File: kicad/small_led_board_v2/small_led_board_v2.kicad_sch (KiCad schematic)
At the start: 89 parts, among them Q1 SQ2351CES, Q2 SQ2351CES, Q3 SQ2351CES, Q4 SQ2351CES, Q5 SQ2351CES, Q6 SQ2351CES, U1 74HCT541, U2 74HCT595, U3 TPIC6B595N

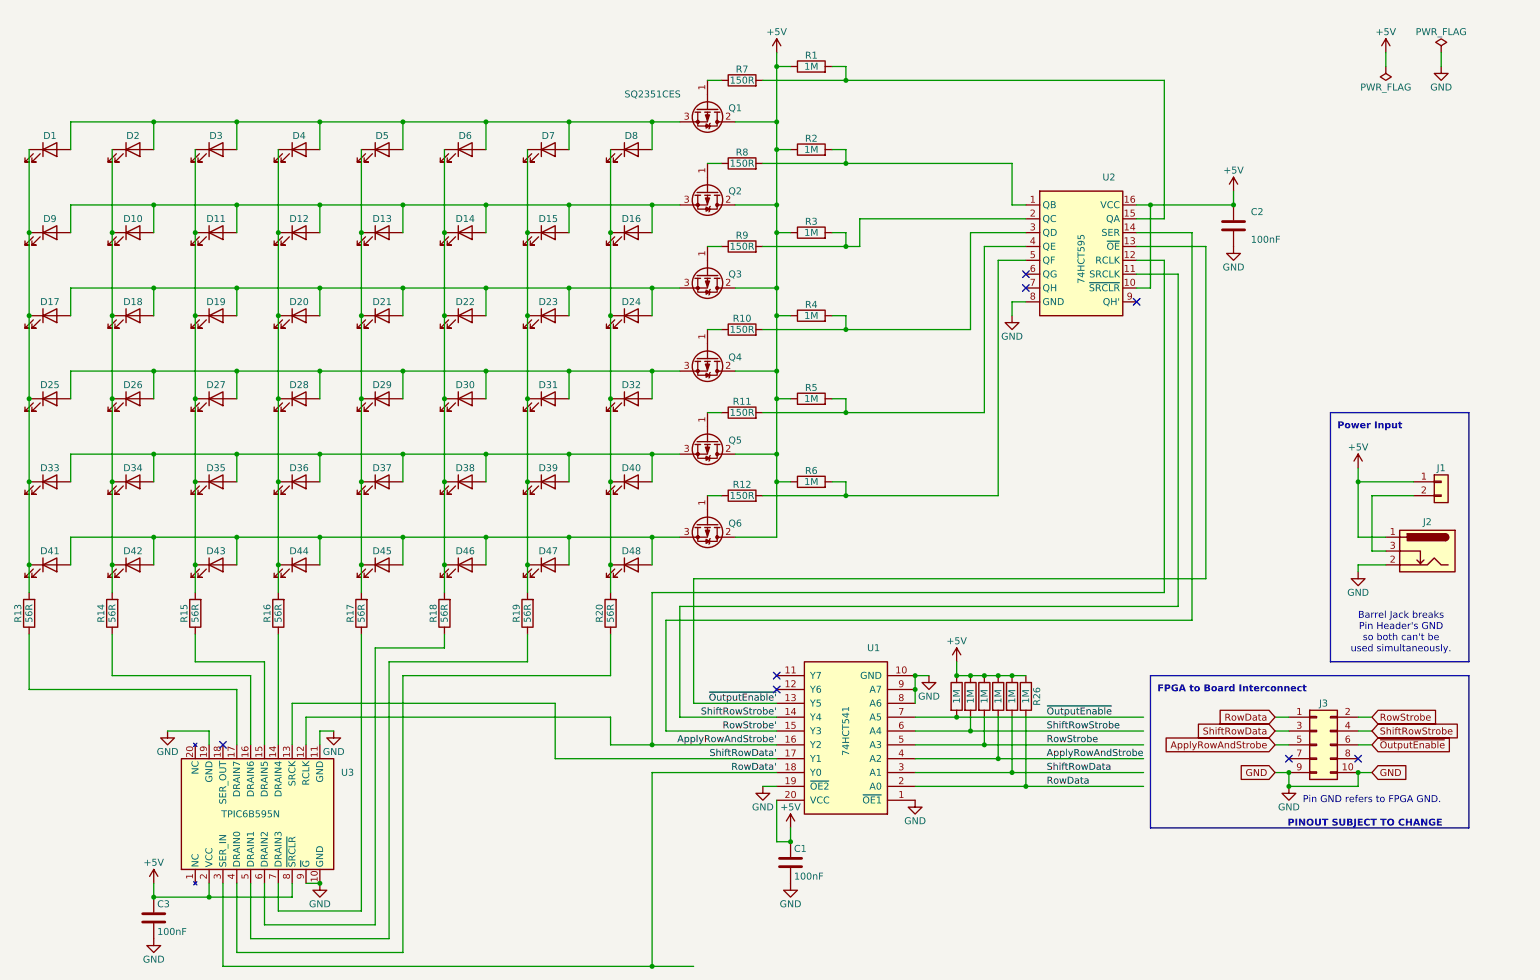
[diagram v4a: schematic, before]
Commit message: small led board v2: replaced rect+text with text box
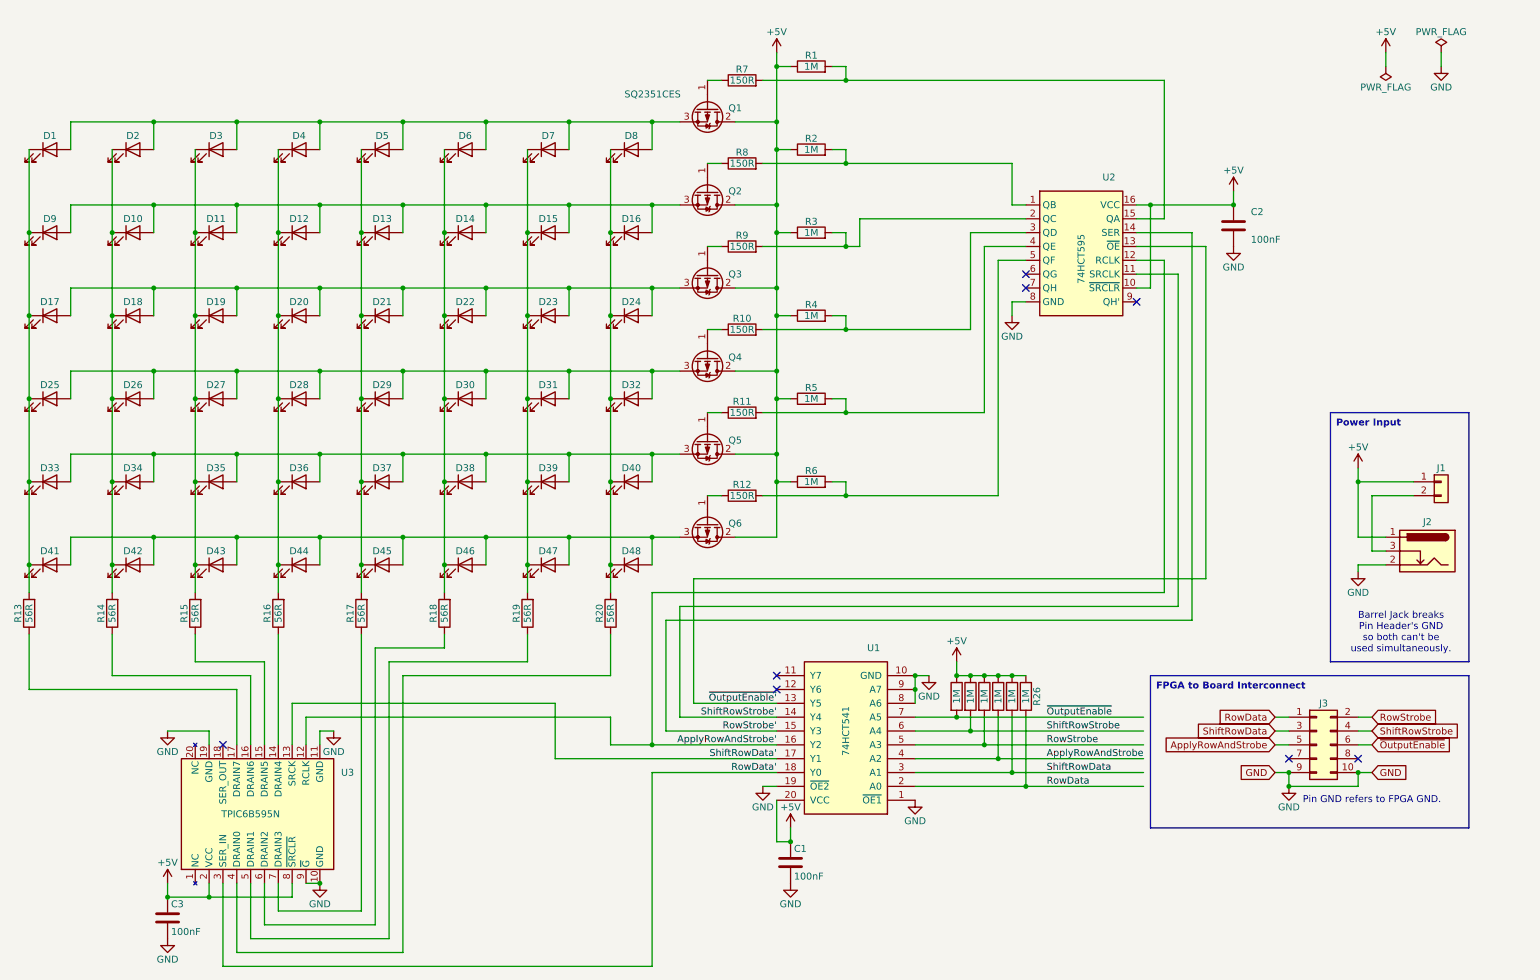
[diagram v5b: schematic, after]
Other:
- note removed: "FPGA to Board Interconnect"
- note removed: "PINOUT SUBJECT TO CHANGE"
- note removed: "Power Input"
- moved on the sheet: C3
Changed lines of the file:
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@@
 	)
 	(junction
-		(at 132.08 187.96)
-		(diameter 0)
-		(color 0 0 0 0)
-	)
-	(junction
 		(at 132.08 109.22)
 		(diameter 0)
@@
 	)
 	(junction
-		(at 40.64 175.26)
+		(at 43.18 175.26)
 		(diameter 0)
 		(color 0 0 0 0)
@@
 	(wire
 		(pts
-			(xy 40.64 172.72) (xy 40.64 175.26)
+			(xy 43.18 172.72) (xy 43.18 175.26)
 		)
 		(stroke
@@
 	(wire
 		(pts
-			(xy 40.64 175.26) (xy 50.8 175.26)
+			(xy 43.18 175.26) (xy 50.8 175.26)
 		)
 		(stroke
@@
 	(wire
 		(pts
-			(xy 132.08 187.96) (xy 139.7 187.96)
-		)
-		(stroke
-			(width 0)
-			(type default)
-		)
-	)
-	(wire
-		(pts
 			(xy 180.34 142.24) (xy 187.96 142.24)
 		)
@@
 		)
 	)
-	(rectangle
-		(start 256.54 86.36)
-		(end 281.94 132.08)
-		(stroke
-			(width 0)
-			(type default)
-		)
-		(fill
-			(type none)
-		)
-	)
-	(rectangle
-		(start 223.52 134.62)
-		(end 281.94 162.56)
+	(text_box "FPGA to Board Interconnect"
+		(exclude_from_sim no)
+		(at 223.52 134.62 0)
+		(size 58.42 27.94)
 		(stroke
 			(width 0)
@@
 			(type none)
 		)
-	)
-	(text "PINOUT SUBJECT TO CHANGE"
-		(exclude_from_sim no)
-		(at 262.89 161.798 0)
 		(effects
 			(font
 				(size 1.27 1.27)
+				(thickness 0.254)
 				(bold yes)
 			)
+			(justify left top)
 		)
 	)
-	(text "Power Input"
+	(text_box "Power Input"
 		(exclude_from_sim no)
-		(at 257.81 88.9 0)
+		(at 256.54 86.36 0)
+		(size 25.4 45.72)
+		(stroke
+			(width 0)
+			(type default)
+		)
+		(fill
+			(type none)
+		)
 		(effects
 			(font
 				(size 1.27 1.27)
-				(thickness 0.254)
 				(bold yes)
 			)
-			(justify left)
+			(justify left top)
 		)
 	)
@@
 		)
 	)
-	(text "FPGA to Board Interconnect"
-		(exclude_from_sim no)
-		(at 224.79 137.16 0)
-		(effects
-			(font
-				(size 1.27 1.27)
-				(thickness 0.254)
-				(bold yes)
-			)
-			(justify left)
-		)
-	)
 	(text "Pin GND refers to FPGA GND."
 		(exclude_from_sim no)
@@
 	(symbol
 		(lib_id "Device:C")
-		(at 40.64 179.07 0)
+		(at 43.18 179.07 0)
 		(unit 1)
 		(exclude_from_sim no)
@@
 		(fields_autoplaced yes)
 		(property "Reference" "C3"
-			(at 41.275 176.53 0)
+			(at 43.815 176.53 0)
 			(effects
 				(font
@@
 		)
 		(property "Value" "100nF"
-			(at 41.275 181.61 0)
+			(at 43.815 181.61 0)
 			(effects
 				(font
@@
 		)
 		(property "Footprint" "Capacitor_THT:C_Disc_D4.7mm_W2.5mm_P5.00mm"
-			(at 41.6052 182.88 0)
+			(at 44.1452 182.88 0)
 			(effects
 				(font
@@
 		)
 		(property "Datasheet" "~"
-			(at 40.64 179.07 0)
+			(at 43.18 179.07 0)
 			(effects
 				(font
@@
 		)
 		(property "Description" "Unpolarized capacitor"
-			(at 40.64 179.07 0)
+			(at 43.18 179.07 0)
 			(effects
 				(font
@@
 	(symbol
 		(lib_id "power:GND")
-		(at 40.64 182.88 0)
+		(at 43.18 182.88 0)
 		(unit 1)
 		(exclude_from_sim no)
@@
 		(fields_autoplaced yes)
 		(property "Reference" "#PWR0115"
-			(at 40.64 189.23 0)
+			(at 43.18 189.23 0)
 			(effects
 				(font
@@
 		)
 		(property "Value" "GND"
-			(at 40.64 186.69 0)
+			(at 43.18 186.69 0)
 			(effects
 				(font
@@
 		)
 		(property "Footprint" ""
-			(at 40.64 182.88 0)
+			(at 43.18 182.88 0)
 			(effects
 				(font
@@
 		)
 		(property "Datasheet" ""
-			(at 40.64 182.88 0)
+			(at 43.18 182.88 0)
 			(effects
 				(font
@@
 		)
 		(property "Description" "Power symbol creates a global label with name \"GND\" , ground"
-			(at 40.64 182.88 0)
+			(at 43.18 182.88 0)
 			(effects
 				(font
@@
 	(symbol
 		(lib_id "power:+5V")
-		(at 40.64 172.72 0)
+		(at 43.18 172.72 0)
 		(unit 1)
 		(exclude_from_sim no)
@@
 		(fields_autoplaced yes)
 		(property "Reference" "#PWR0114"
-			(at 40.64 176.53 0)
+			(at 43.18 176.53 0)
 			(effects
 				(font
@@
 		)
 		(property "Value" "+5V"
-			(at 40.64 168.91 0)
+			(at 43.18 168.91 0)
 			(effects
 				(font
@@
 		)
 		(property "Footprint" ""
-			(at 40.64 172.72 0)
+			(at 43.18 172.72 0)
 			(effects
 				(font
@@
 		)
 		(property "Datasheet" ""
-			(at 40.64 172.72 0)
+			(at 43.18 172.72 0)
 			(effects
 				(font
@@
 		)
 		(property "Description" "Power symbol creates a global label with name \"+5V\""
-			(at 40.64 172.72 0)
+			(at 43.18 172.72 0)
 			(effects
 				(font

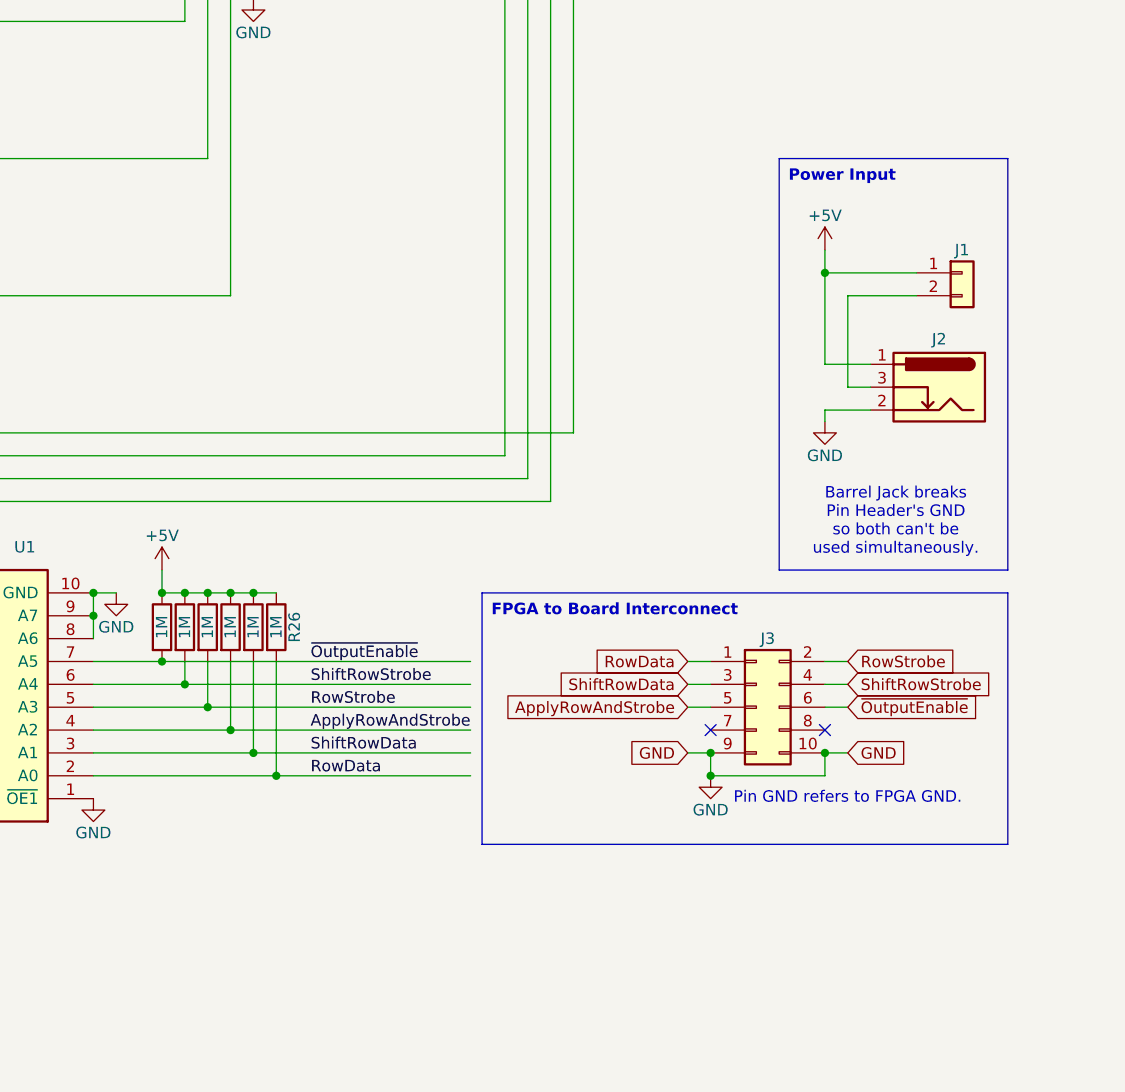
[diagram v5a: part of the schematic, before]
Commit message: kicad: migration complete to 9.0, small led boards both done
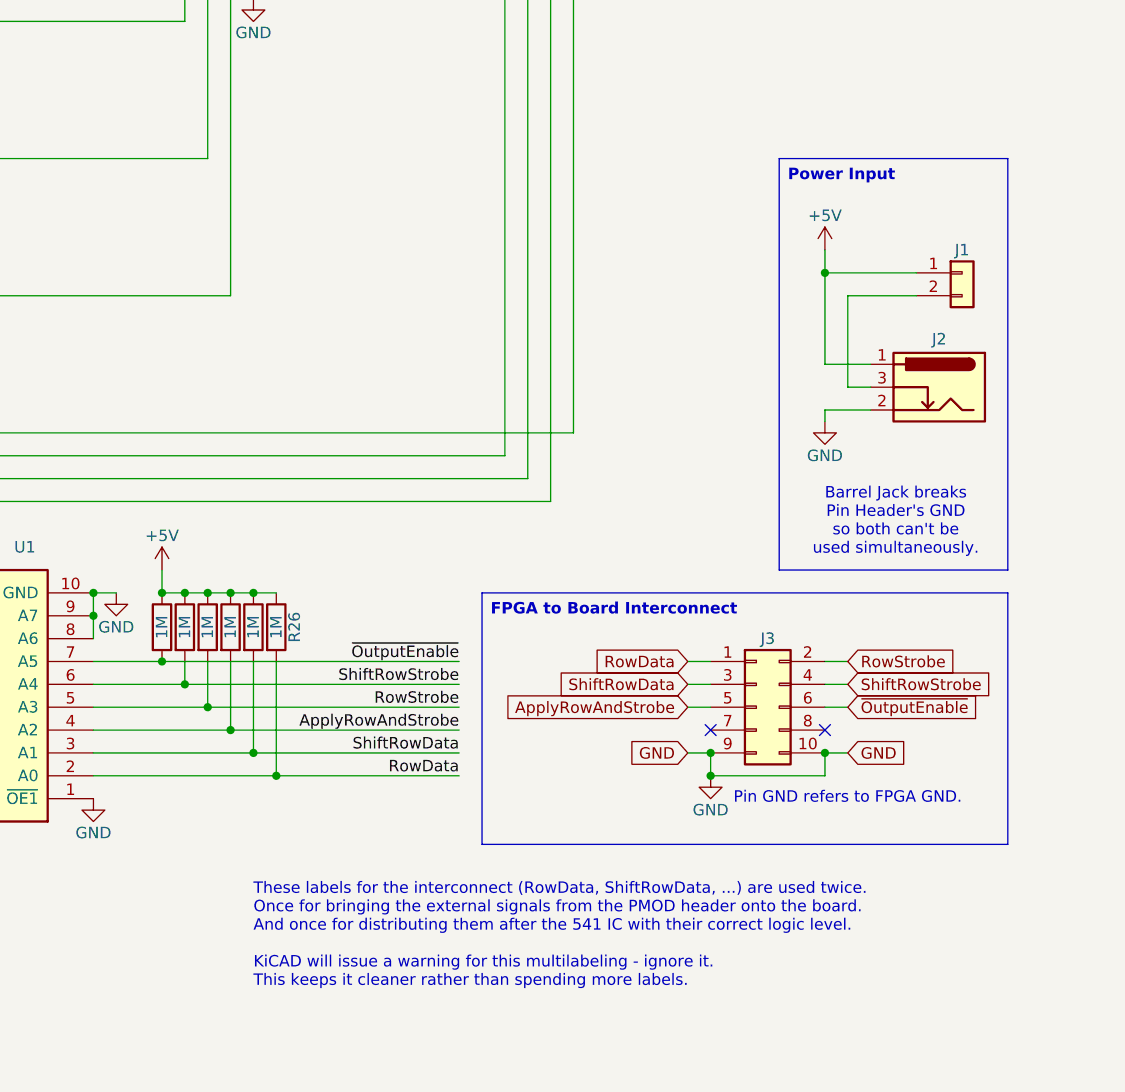
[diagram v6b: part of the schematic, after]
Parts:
- removed Q1, Q2, Q3, Q4, Q5, Q6: SQ2351CES, Package_TO_SOT_SMD:SOT-23-3, symbol Transistor_FET:IRF4905
- removed U1: 74HCT541, Package_DIP:DIP-20_W7.62mm, symbol 74xx:74AHCT541
- removed U2: 74HCT595, Package_SO:SOIC-16_3.9x9.9mm_P1.27mm, symbol 74xx:74HCT595
- removed U3: TPIC6B595N, Package_DIP:DIP-20_W7.62mm, symbol Interface_Expansion:TPIC6595
- added Q1, Q2, Q3, Q4, Q5, Q6: SQ2351CES, Package_TO_SOT_SMD:SOT-23-3, symbol symbol_library:SQ2351CES
- added U1: 74HCT541, Package_DIP:DIP-20_W7.62mm, symbol symbol_library:74HCT541
- added U2: 74HCT595, Package_SO:SOIC-16_3.9x9.9mm_P1.27mm, symbol symbol_library:74HCT595
- added U3: TPIC6B595N, Package_DIP:DIP-20_W7.62mm, symbol symbol_library:TPIC6B595N
- D1, D10, D11, D12, D13, D14, D15, D16, D17, D18, D19, D2, D20, D21, D22, D23, D24, D25, D26, D27, D28, D29, D3, D30, D31, D32, D33, D34, D35, D36, D37, D38, D39, D4, D40, D41, D42, D43, D44, D45, D46, D47, D48, D5, D6, D7, D8, D9: value ~ -> LED
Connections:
- net +5V: now also Q1.2 (S), Q2.2 (S), Q3.2 (S), Q4.2 (S), Q5.2 (S), Q6.2 (S), U1.20 (VCC), U2.10 (~{SRCLR}), U2.16 (VCC), U3.2 (VCC), U3.8 (~{SRCLR})
- net ApplyRowAndStrobe: now also U1.4 (A2)
- net ApplyRowAndStrobe': now also U1.16 (Y2), U2.12 (RCLK), U3.12 (RCLK)
- net GND: now also U1.1 (~{OE1}), U1.10 (GND), U1.19 (~{OE2}), U1.8 (A6), U1.9 (A7), U2.8 (GND), U3.10 (GND), U3.11 (GND), U3.19 (GND), U3.9 (~{G})
- net RowData: now also U1.2 (A0)
- net RowData': now also U1.18 (Y0), U3.3 (SER_IN)
- net RowStrobe: now also U1.5 (A3)
- net RowStrobe': now also U1.15 (Y3), U2.14 (SER)
- net ShiftRowData: now also U1.3 (A1)
- net ShiftRowData': now also U1.17 (Y1), U3.13 (SRCK)
- net ShiftRowStrobe: now also U1.6 (A4)
- net ShiftRowStrobe': now also U1.14 (Y4), U2.11 (SRCLK)
- net ~{OutputEnable'}: now also U1.13 (Y5), U2.13 (~{OE})
- net ~{OutputEnable}: now also U1.7 (A5)
- net at D1.2 (A), D2.2 (A), D3.2 (A)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: now also Q1.3 (D)
- net at R10.1: now also Q4.1 (G)
- net at D25.2 (A), D26.2 (A), D27.2 (A)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: now also Q4.3 (D)
- net at D41.2 (A), D42.2 (A), D43.2 (A)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: now also Q6.3 (D)
- net at R7.1: now also Q1.1 (G)
- net at R1.2, R7.2: now also U2.15 (QA)
- net at R3.2, R9.2: now also U2.2 (QC)
- net at R15.1: now also U3.15 (DRAIN5)
- net at D33.2 (A), D34.2 (A), D35.2 (A)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: now also Q5.3 (D)
- net at R2.2, R8.2: now also U2.1 (QB)
- net at D17.2 (A), D18.2 (A), D19.2 (A)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: now also Q3.3 (D)
- net at R8.1: now also Q2.1 (G)
- net at D10.2 (A), D11.2 (A), D12.2 (A)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: now also Q2.3 (D)
- net at R12.2, R6.2: now also U2.5 (QF)
- net at R16.1: now also U3.14 (DRAIN4)
- net at R14.1: now also U3.16 (DRAIN6)
- net at R13.1: now also U3.17 (DRAIN7)
- net at R20.1: now also U3.4 (DRAIN0)
- net at R19.1: now also U3.5 (DRAIN1)
- net at R18.1: now also U3.6 (DRAIN2)
- net at R17.1: now also U3.7 (DRAIN3)
- net at R9.1: now also Q3.1 (G)
- net at R10.2, R4.2: now also U2.3 (QD)
- net at R11.2, R5.2: now also U2.4 (QE)
- net at R11.1: now also Q5.1 (G)
- net at R12.1: now also Q6.1 (G)
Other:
- note added: "These labels for the interconnect (RowData, ShiftRowData, ...) are used twice. Once for bringing the external signals from the PMOD header onto the board. And once for distributing them after the 541 IC with their correct logic level. KiCAD will issue a warning for this multilabeling - ignore it. This keeps it cleaner rather than spending more labels."

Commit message: small led board v2: moved buffer pullups to +3.3v of pmod
This was a serious design oversight of not paying attention that the pullups could inject current into the FPGA IO when it's driven high (3.3V).
The only reason the FPGA survived this for so long is that the current was significantly limited by the pullups (10K/1M results in way too weak current) and an internal ESD diode possibly clamped the current.

The fullsize board is also affected and will be fixed in the next commit.
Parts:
- removed J3: ~, Connector_PinHeader_2.54mm:PinHeader_2x05_P2.54mm_Horizontal, symbol Connector_Generic:Conn_02x05_Odd_Even
- added J3: ~, Connector_PinHeader_2.54mm:PinHeader_2x06_P2.54mm_Horizontal, symbol Connector_Generic:Conn_02x06_Odd_Even
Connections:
- net +5V: no longer R21.1, R22.1, R23.1, R24.1, R25.1, R26.1
- net ApplyRowAndStrobe: now also J3.5 (Pin_5)
- net GND: now also J3.10 (Pin_10), J3.9 (Pin_9)
- net RowData: now also J3.1 (Pin_1)
- net RowStrobe: now also J3.2 (Pin_2)
- net ShiftRowData: now also J3.3 (Pin_3)
- net ShiftRowStrobe: now also J3.4 (Pin_4)
- net ~{OutputEnable}: now also J3.6 (Pin_6)
- new net 3.3V: J3.11 (Pin_11), J3.12 (Pin_12), R21.1, R22.1, R23.1, R24.1, R25.1, R26.1
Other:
- note removed: "Pin GND refers to FPGA GND."
